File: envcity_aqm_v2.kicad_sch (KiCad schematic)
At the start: 113 parts, among them IC1 DS1307ZN+, IC2 DMMT5401-7F, IC3 DMMT5401-7F, IC4 DMMT5401-7-F, J10 Conn_01x03_Male, J11 Conn_01x04_Male, J12 Conn_01x02_Male, J13 Conn_01x02_Male, J14 Micro_SD_Card, J2 Screw_Terminal_01x02, J3 Screw_Terminal_01x02, J4 Conn_01x06_Male, J5 Conn_01x06_Male, J6 Conn_01x06_Male, J7 Conn_01x06_Male, J8 USB_B_Micro, Q1 DMG2301L, Q12 DMG2301L / DMP2045U, Q13 DMN10H220L, Q14 DMN10H220L, Q2 DMG2301L, Q5 DMG2301L / DMP2045U, Q8 DMG2301L, Q9 DMG2301L / DMP2045U, SW1 RESET, U1 ADS1115IDGS, U2 CD74HC4067M, U3 ESP32-C3-MINI-1-N4, U4 LM2596S-5, U5 TP4056, U6 MT3608, U7 MT3608, U8 DHT11, U9 USBLC6-2SC6, Y1 32,768KHz

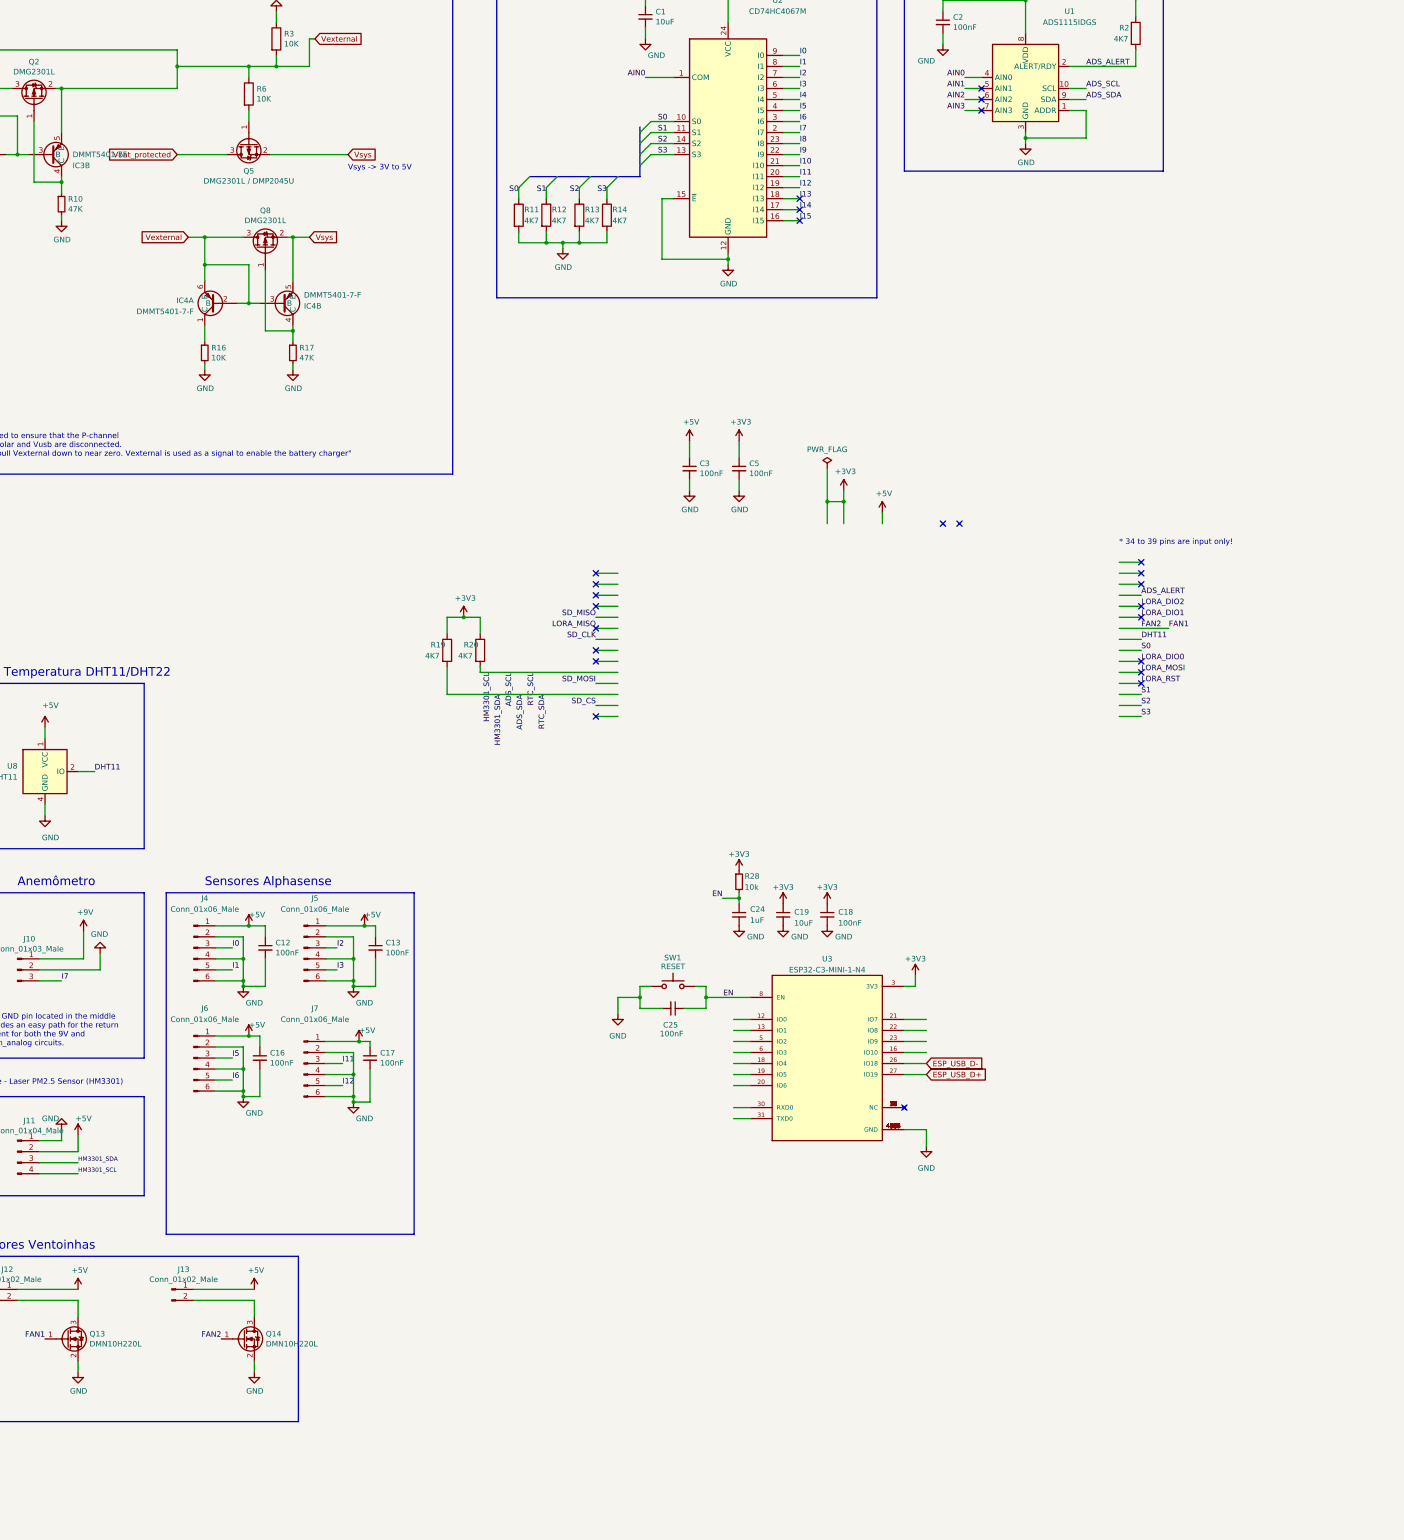
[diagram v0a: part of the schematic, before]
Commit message: add rfm95
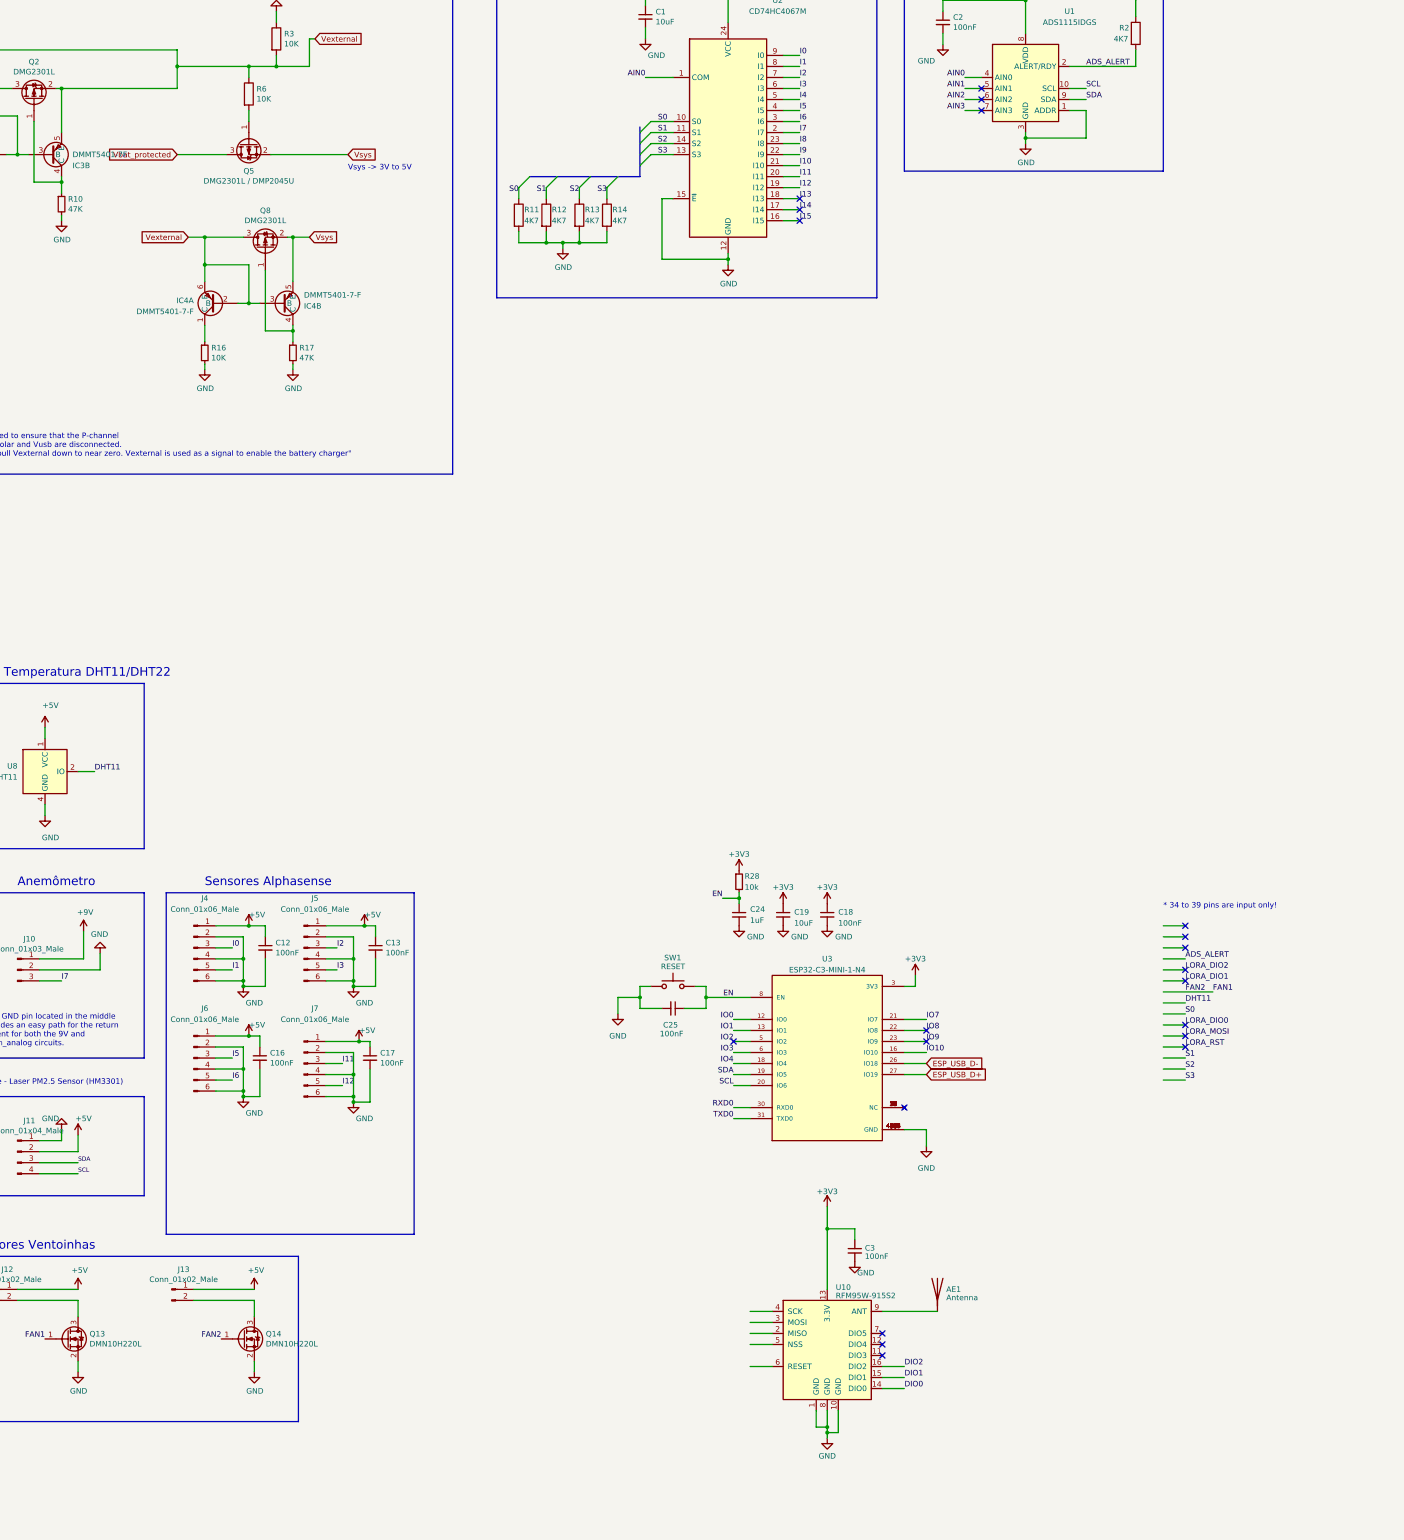
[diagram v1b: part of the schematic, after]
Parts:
- removed C5: 100nF, Capacitor_SMD:C_0805_2012Metric_Pad1.15x1.40mm_HandSolder, symbol Device:C_Small
- removed R19, R20: 4K7, Resistor_SMD:R_0805_2012Metric_Pad1.15x1.40mm_HandSolder, symbol Device:R
- added AE1: Antenna, symbol Device:Antenna
- added U10: RFM95W-915S2, symbol RF_Module:RFM95W-915S2
- C3: footprint Capacitor_SMD:C_0805_2012Metric_Pad1.15x1.40mm_HandSolder -> (none)
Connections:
- net +3V3: now also C3.1, U10.13 (3.3V)
- net +5V: no longer C3.1
- net GND: now also U10.1 (GND), U10.10 (GND), U10.8 (GND)
- net IO0: now reaches U3.12 (IO0)
- net IO1: now reaches U3.13 (IO1)
- net IO10: now reaches U3.16 (IO10)
- net IO4: now reaches U3.18 (IO4)
- net SDA: now reaches U3.19 (IO5)
- net SDA: now also J11.3 (Pin_3), U1.9 (SDA)
- net SCL: now reaches U3.20 (IO6)
- net SCL: now also J11.4 (Pin_4), U1.10 (SCL)
- net IO7: now reaches U3.21 (IO7)
- net IO8: now reaches U3.22 (IO8)
- net IO9: now reaches U3.23 (IO9)
- net RXD0: now reaches U3.30 (RXD0)
- net TXD0: now reaches U3.31 (TXD0)
- net IO2: now reaches U3.5 (IO2)
- net IO3: now reaches U3.6 (IO3)
- removed net ADS_SCL: IC1.6 (SCL), J11.4 (Pin_4), U1.10 (SCL)
- removed net ADS_SDA: IC1.5 (SDA), J11.3 (Pin_3), U1.9 (SDA)
- new net: AE1.1 (A), U10.9 (ANT)
- new net DIO0: U10.14 (DIO0)
- new net DIO1: U10.15 (DIO1)
- new net DIO2: U10.16 (DIO2)
- new net RTC_SCL: IC1.6 (SCL)
- new net RTC_SDA: IC1.5 (SDA)
- no-connect marks 29 -> 25

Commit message: Add conversor 3v3. Add rfm. Changing esp32c3-mini to esp32-s2
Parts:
- removed U3: ESP32-C3-MINI-1-N4, ESP32-C3-MINI-1-N4:XCVR_ESP32-C3-MINI-1-N4, symbol ESP32-C3-MINI-1-N4:ESP32-C3-MINI-1-N4
- added C26, C5: 10uF, Capacitor_SMD:C_0603_1608Metric, symbol Device:C
- added C27: 100nF, Capacitor_SMD:C_0603_1608Metric, symbol Device:C
- added D15: LED, LED_SMD:LED_0603_1608Metric, symbol Device:LED
- added IC5: ESP32-S2-SOLO-N4R2, ESP32S2SOLON4R2, symbol ESP32-S2-SOLO-N4R2:ESP32-S2-SOLO-N4R2
- added R19, R20: 4K7, symbol Device:R_Small
- added R29: 10k, Resistor_SMD:R_0603_1608Metric, symbol Device:R_US
- added R30: 100k, Resistor_SMD:R_0603_1608Metric, symbol Device:R_US
- added SW1: BOOT, Button_Switch_SMD:SW_SPST_PTS810, symbol Switch:SW_Push
- added U11: AP2112K-3.3, Package_TO_SOT_SMD:SOT-23-5, symbol Regulator_Linear:AP2112K-3.3
- C19: value 10uF -> 22uF
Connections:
- net RTC_SCL is gone; now on net SCL: IC1.6 (SCL)
- net RTC_SDA is gone; now on net SDA: IC1.5 (SDA)
- net +3V3: now also C26.1, C27.1, C5.1, IC5.2 (3V3), R19.1, R20.1, U11.5 (VOUT)
- net +5V: now also R29.1, R30.1, U11.1 (VIN)
- net EN: now also IC5.3 (EN)
- net ESP_USB_D+: now also IC5.14 (IO20)
- net ESP_USB_D-: now also IC5.13 (IO19)
- net FAN1: now also IC5.38 (IO2); no longer Q14.1 (G)
- net GND: now also C26.2, C27.2, C5.2, D15.1 (K), IC5.1 (GND_1), IC5.40 (GND_2), IC5.41 (GND_3), IC5.42 (GND_4), IC5.43 (GND_5), IC5.44 (GND_6), IC5.45 (GND_7), IC5.46 (GND_8), IC5.47 (GND_9), IC5.48 (GND_10), IC5.49 (GND_11), SW1.2, U11.2 (GND)
- net I11: no longer J7.3 (Pin_3)
- net I12: no longer J7.5 (Pin_5)
- net I4: now also J6.3 (Pin_3)
- net I5: now also J6.5 (Pin_5); no longer J6.3 (Pin_3)
- net I6: now also J7.3 (Pin_3); no longer J6.5 (Pin_5)
- net I7: now also J7.5 (Pin_5)
- net S0: now also IC5.4 (IO4)
- net S1: now also IC5.5 (IO5)
- net S2: now also IC5.6 (IO6)
- net S3: now also IC5.7 (IO7)
- net SCL: now also IC5.32 (IO39), R20.2
- net SDA: now also IC5.31 (IO38), R19.2
- net SD_CS: now also IC5.10 (IO17)
- net SD_MISO: now also IC5.9 (IO16)
- net SD_MOSI: now also IC5.8 (IO15)
- net RFM_MISO: now reaches U10.2 (MISO)
- net RFM_MISO: now also IC5.18 (IO10)
- net RFM_MOSI: now reaches U10.3 (MOSI)
- net RFM_MOSI: now also IC5.19 (IO11)
- net RFM_SCK: now reaches U10.4 (SCK)
- net RFM_SCK: now also IC5.20 (IO12)
- net RFM_CS: now reaches U10.5 (NSS)
- net RFM_CS: now also IC5.21 (IO13)
- net RFM_RST: now reaches U10.6 (RESET)
- net RFM_RST: now also IC5.22 (IO14)
- net DHT11 renamed DHT_PIN
- net DHT_PIN: now also IC5.35 (IO42)
- net DIO0 renamed RFM_DIO0
- net RFM_DIO0: now also IC5.23 (IO21)
- net DIO1 renamed RFM_DIO1
- net RFM_DIO1: now also IC5.24 (IO33)
- net DIO2 renamed RFM_DIO2
- net RFM_DIO2: now also IC5.25 (IO34)
- net SD_CLK renamed SD_SCK
- net SD_SCK: now also IC5.11 (IO18)
- net SD_Data1: no longer names the net of J14.8 (DAT1)
- net SD_Data2: no longer names the net of J14.1 (DAT2)
- new net: R30.2, U11.3 (EN)
- new net: D15.2 (A), R29.2
- new net: IC5.27 (IO0), SW1.1
- new net FAN2: IC5.39 (IO1), Q14.1 (G)
- no-connect marks 25 -> 12
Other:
- note added: "* Verificar simulações Power-Path * Alterar transitors para o DMMT - OK * Alterações Marcio: * Entradas analógicas an1...an3 expostas * ESP32-C3 - ok * Dissipador onboard - Verificar * Regulador 3V3 (Lembrar que radio + esp32)"
- note added: "Conversor Linear 3V3"
- note added: "Pin Map: 1. ADS 2. SCL 3. MUX_SO 4. MUX_S1 5. MUX_S2 6. MUX_S3 7. MISO 8. MOSI 9. SCK 10. CS 11. DIO0 12. DIO1 13. DIO2 14. FAN1 15. FAN2 16. DHT22 - Temperatura e Umidade 17. MISO 18. MOSI 19. SCK 20. CS"
- note removed: "* Verificar simulações Power-Path * Alterar transitors para o DMMT * Alterações Marcio: * Entradas analógicas an1...an3 expostas * ESP32-C3 * Dissipador onboard - Verificar"
- note removed: "Checklist Pinos: ADS: ok SENSORES: ok MUX: ok SD: Conectado, porem necessita verificar se funciona Ventoinhas: OK"
- moved on the sheet: AE1, C1, C14, C15, C18, C19, C2, C20, C21, C24, C25, C3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

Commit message: separa a alimentacao do esp32 e do rfm. add 2 conectores para alphasense. Add conector pms5003
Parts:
- added C28, C29, C30: 100nF, Capacitor_SMD:C_0805_2012Metric_Pad1.15x1.40mm_HandSolder, symbol Device:C_Small
- added C31, C32: 10uF, Capacitor_SMD:C_0603_1608Metric, symbol Device:C
- added C33: 100nF, Capacitor_SMD:C_0603_1608Metric, symbol Device:C
- added D16: LED, LED_SMD:LED_0603_1608Metric, symbol Device:LED
- added J1, J9: Conn_01x06_Male, Connector_Molex:Molex_KK-254_AE-6410-06A_1x06_P2.54mm_Vertical, symbol envcity_aqm_v2-rescue:Conn_01x06_Male-Connector
- added J15: Conn_01x08_Pin, symbol Connector:Conn_01x08_Pin
- added R34, R35: 10k, symbol Device:R_Small
- added R36: 10k, Resistor_SMD:R_0603_1608Metric, symbol Device:R_US
- added R37: 100k, Resistor_SMD:R_0603_1608Metric, symbol Device:R_US
- added U3: AP2112K-3.3, Package_TO_SOT_SMD:SOT-23-5, symbol Regulator_Linear:AP2112K-3.3
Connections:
- net +3V3: now also R34.1, R35.1; no longer C3.1, U10.13 (3.3V)
- net +5V: now also C28.1, C29.1, C30.1, J1.1 (Pin_1), J15.1 (Pin_1), J9.1 (Pin_1), R36.1, R37.1, U3.1 (VIN)
- net GND: now also C28.2, C29.2, C30.2, C31.2, C32.2, C33.2, D16.1 (K), J1.2 (Pin_2), J1.4 (Pin_4), J1.6 (Pin_6), J15.2 (Pin_2), J9.2 (Pin_2), J9.4 (Pin_4), J9.6 (Pin_6), U3.2 (GND)
- net I10: now also J9.3 (Pin_3)
- net I11: now also J9.5 (Pin_5)
- net I8: now also J1.3 (Pin_3)
- net I9: now also J1.5 (Pin_5)
- net PMS_TX: now reaches IC5.36 (RXD0)
- net PMS_TX: now also J15.5 (Pin_5)
- net PMS_RX: now reaches IC5.37 (TXD0)
- net PMS_RX: now also J15.4 (Pin_4)
- new net: D16.2 (A), R36.2
- new net: R37.2, U3.3 (EN)
- new net 3V3-RFM: C3.1, C31.1, C32.1, C33.1, U10.13 (3.3V), U3.5 (VOUT)
- new net RESET: J15.6 (Pin_6), R35.2
- new net SET: J15.3 (Pin_3), R34.2
- no-connect marks 12 -> 15
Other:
- note added: "* Verificar simulações Power-Path * Alterar transitors para o DMMT - OK * Alterações Marcio: * Entradas analógicas an1...an3 expostas * Adicionado + 2 conectores p/ alphasense * Falta expor ANx... * ESP32-C3 - ok * Dissipador onboard - Verificar * Regulador 3V3 * Um regulador para o esp32 e um para o rfm * ADD PMS5003 - ok"
- note added: "Conversor Linear 3V3 - ESP32"
- note added: "Conversor Linear 3V3 - RFM95"
- note added: "ESP32-S2-WROOM"
- note added: "LoRa-RFM95"
- note added: "PMS5003"
- note added: "Sensor DHT11/DHT22"
- note removed: "* 34 to 39 pins are input only!"
- note removed: "* Verificar simulações Power-Path * Alterar transitors para o DMMT - OK * Alterações Marcio: * Entradas analógicas an1...an3 expostas * ESP32-C3 - ok * Dissipador onboard - Verificar * Regulador 3V3 (Lembrar que radio + esp32)"
- note removed: "Conversor Linear 3V3"
- note removed: "R1 = 14R2"
- note removed: "Sensor de Temperatura DHT11/DHT22"
- moved on the sheet: AE1, C1, C12, C13, C16, C17, C18, C19, C2, C24, C25, C3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
